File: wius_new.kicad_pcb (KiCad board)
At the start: 6 copper layers, 54 x 28 mm, 134 parts, among them IC1 BQ24040DSQT, J2 52746-1271, J3 1040310811, J4 SS5-10-3.00-L-D-K-TR, J5 USB4745-03-A, J8 2, J9 U.FL, M1 MountingHole_Pad, M2 MountingHole_Pad, M3 MountingHole_Pad, M4 MountingHole_Pad, SW3 Button Switch SPST-No, SW4 Button Switch SPST-No, U1 TPS62840YBGR, U12 SN74LVC1T45DCK, U13 TXB0104RUT, U2 TXB0104RUT, U3 SiWG917Y, U4 FT232HPQ, U5 LSM6DSV, U6 SN74AXC4T774RSVR, U7 SOIC_clipProgSmall, U8 TXB0104RUT, U9 PCAL6408AHK, Y1 SIT1552AI-JE-DCC-32.768E

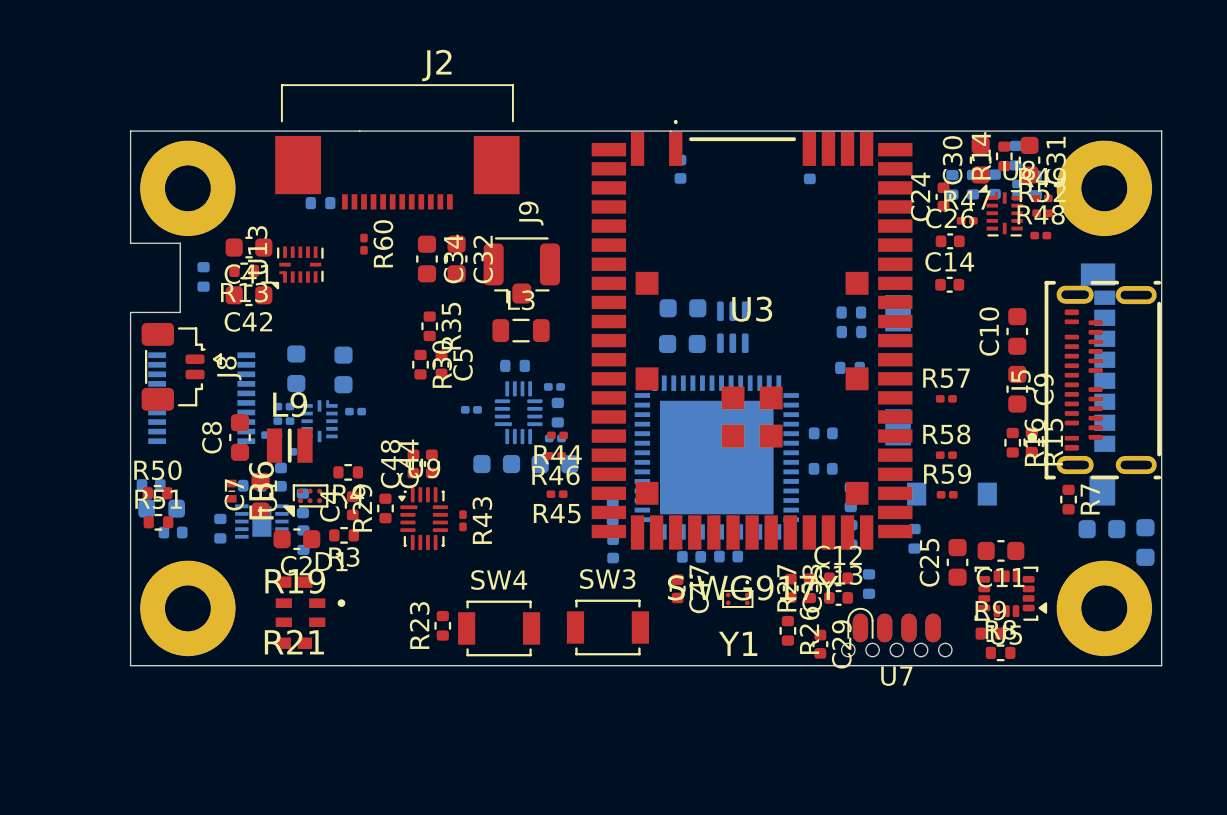
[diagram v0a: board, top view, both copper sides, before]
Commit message: initial routing of SPI, USB and Power
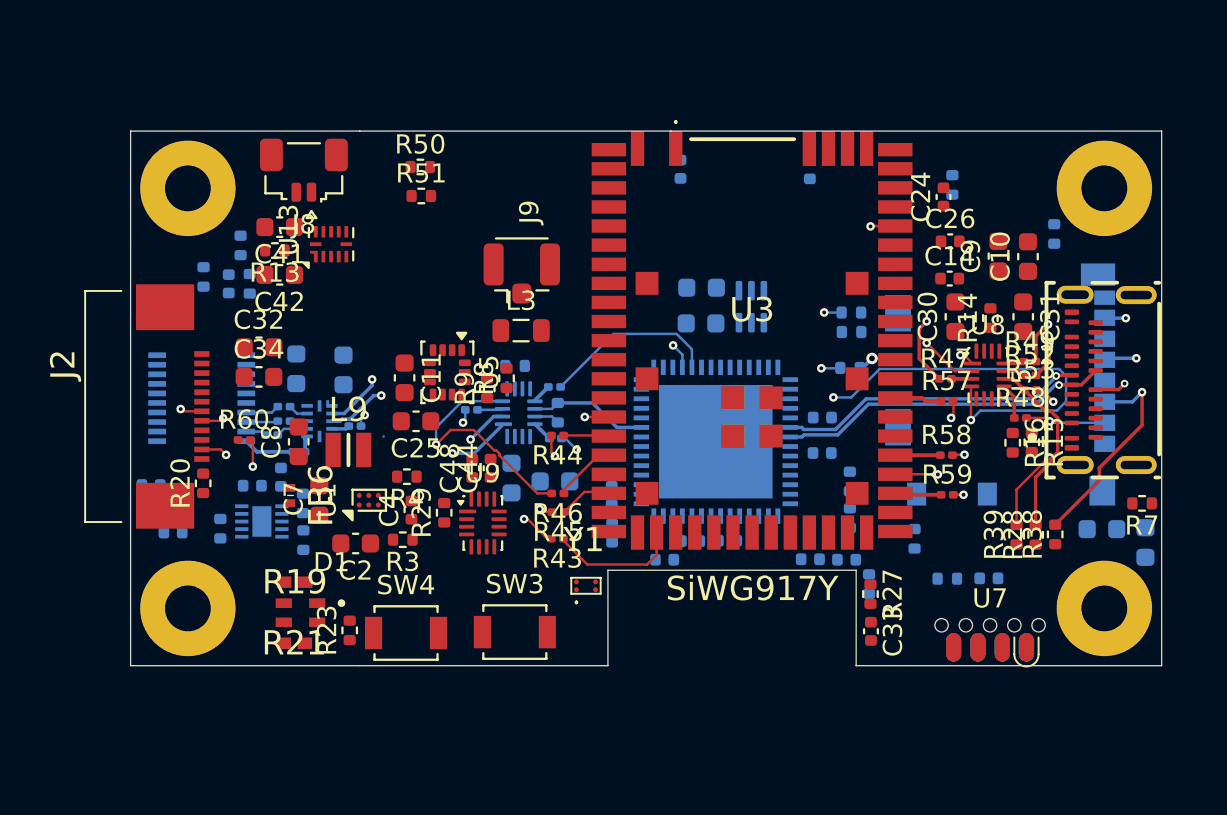
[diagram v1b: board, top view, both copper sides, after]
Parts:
- removed R40: 100k, Resistor_SMD:R_0402_1005Metric
- added R28: 10k, Resistor_SMD:R_0402_1005Metric, F.Cu at (170.4, 107.2)
- C12, C13, C29, C47, C5, R26, R30, R35: moved to B.Cu
- R20, R53: moved to F.Cu
- R38, R39: value 100k -> 10k; moved to F.Cu
- U8: value TXB0104RUT -> SN74AXC4T774RSVR; footprint Package_DFN_QFN:Texas_R-PUQFN-N12 -> Package_DFN_QFN:UQFN-16_1.8x2.6mm_P0.4mm
- moved C11 32.5 mm to (137.3, 98.9), turned to -90 degrees
- moved U5 31.5 mm to (139.6, 98.6), turned to -90 degrees
- moved R8 29.6 mm to (142.7, 98.9), turned to 90 degrees
- moved R9 29.3 mm to (141.7, 99.5), turned to 90 degrees
- moved C25 29.3 mm to (137.9, 101.2), turned to 180 degrees
- moved R50 21.9 mm to (138.2, 87.9)
- moved R51 21.9 mm to (138.2, 89.4)
- moved R38 19.9 mm to (171.4, 107.1), turned to 90 degrees
- moved J2 19.1 mm to (123.7, 100.4), turned to -90 degrees
- moved R39 18.4 mm to (169.4, 107.1), turned to 90 degrees
- moved R20 15.9 mm to (126.8, 104.5), turned to 90 degrees
- moved J8 12.4 mm to (132.1, 88.0), turned to 180 degrees
- moved R60 12.0 mm to (128.9, 102.2), turned to 0 degrees
- moved C5 11.9 mm to (128.1, 94.0)
- moved C32 11.3 mm to (129.7, 97.3), turned to 0 degrees
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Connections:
- R14 pad 1: /IMU_SD/SD_EN -> VIO
- R14 pad 2: GND -> /IMU_SD/SD_EN
- R38 pad 2: /IMU_SD/SPI_SD.MISO -> /IMU_SD/SPI_SD.MOSI
- R39 pad 2: /IMU_SD/SPI_SD.MOSI -> /IMU_SD/SPI_SD.CS0
- U8 pad 1: VIO -> /IMU_SD/SPI_MCU.SCK
- U8 pad 10: Net-(U8-B1) -> /IMU_SD/SPI_SD.MISO
- U8 pad 11: 3V3_VBUS -> Net-(U8-B2)
- U8 pad 12: /IMU_SD/SD_EN -> Net-(U8-B1)
- U8 pad 2: /IMU_SD/SPI_MCU.SCK -> /IMU_SD/SPI_MCU.MOSI
- U8 pad 3: /IMU_SD/SPI_MCU.MOSI -> Net-(U8-A3)
- U8 pad 4: Net-(U8-A3) -> /IMU_SD/SPI_MCU.CS0
- U8 pad 5: /IMU_SD/SPI_MCU.CS0 -> GND
- U8 pad 6: GND -> VIO
- U8 pad 7: Net-(U8-B4) -> /IMU_SD/SD_EN
- U8 pad 8: /IMU_SD/SPI_SD.MISO -> GND
- U8 pad 9: Net-(U8-B2) -> Net-(U8-B4)
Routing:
- net 3V3_VBUS: track 0.00 -> 95.7 mm
- net VIO: track 0.00 -> 86.8 mm
- net /MCU/ULP_SSI.CS0: track 0.00 -> 55.0 mm, vias 0 -> 2
- net 1V8: track 0.00 -> 49.5 mm
- net /MCU/ULP_SSI.SCK: track 0.00 -> 45.4 mm, vias 0 -> 2
- net /MCU/ULP_SSI.MOSI: track 0.00 -> 44.7 mm, vias 0 -> 2
- net /MCU/ULP_SSI.MISO: track 0.00 -> 43.5 mm, vias 0 -> 2
- net /IMU_SD/SPI_MCU.CS0: track 0.00 -> 38.8 mm, vias 0 -> 3
- net /IMU_SD/SPI_MCU.SCK: track 0.00 -> 38.2 mm, vias 0 -> 3
- net /IMU_SD/SPI_MCU.MOSI: track 0.00 -> 34.9 mm, vias 0 -> 3
- net 5V: track 0.00 -> 34.6 mm
- net /IMU_SD/SPI_MCU.MISO: track 0.00 -> 34.3 mm, vias 0 -> 3
- net /MCU/SPI_FPGA.MISO: track 0.00 -> 34.2 mm, vias 0 -> 2
- net /MCU/SPI_FPGA.MOSI: track 0.00 -> 32.6 mm, vias 0 -> 2
- net /MCU/SPI_FPGA.SCK: track 0.00 -> 30.2 mm, vias 0 -> 2
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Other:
- outline, holes or cut-outs redrawn

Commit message: Comments on layout
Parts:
- removed U5: LSM6DSV, Package_LGA:LGA-14_3x2.5mm_P0.5mm_LayoutBorder3x4y
- J2: moved to B.Cu
- moved J2 43.9 mm to (165.5, 87.0), turned to 0 degrees
- moved R60 40.6 mm to (167.4, 89.2)
- moved R23 30.9 mm to (164.8, 118.0)
- moved SW4 28.5 mm to (165.6, 108.1), turned to 180 degrees
- moved U12 18.0 mm to (169.3, 83.6)
- moved C37 18.0 mm to (166.7, 82.6)
- moved C38 18.0 mm to (166.7, 84.5)
- moved R54 17.4 mm to (157.5, 95.8), turned to 180 degrees
- moved C47 13.2 mm to (157.6, 97.0), turned to 0 degrees
- moved U6 12.8 mm to (155.1, 95.6), turned to 180 degrees
- moved R31 12.1 mm to (155.2, 98.0), turned to 180 degrees
- moved R38 11.2 mm to (170.4, 96.0), turned to -90 degrees
- moved R55 11.1 mm to (153.1, 94.2), turned to 180 degrees
- moved R16 10.8 mm to (174.4, 92.9), turned to 90 degrees
- moved R15 9.93 mm to (173.4, 92.9), turned to 90 degrees
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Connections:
- R32 pad 1: /MCU/SPI_FPGA.MOSI -> /IMU_SD/SPI_MCU.MOSI
- R33 pad 1: /MCU/SPI_FPGA.SCK -> /IMU_SD/SPI_MCU.SCK
- R34 pad 1: /MCU/SPI_FPGA.CS0 -> /IMU_SD/SPI_MCU.CS0
- R43 pad 2: /IMU_SD/SPI_MCU.SCK -> /MCU/SPI_FPGA.SCK
- R44 pad 2: /IMU_SD/SPI_MCU.CS0 -> /MCU/SPI_FPGA.CS0
- R45 pad 2: /IMU_SD/SPI_MCU.MOSI -> /MCU/SPI_FPGA.MOSI
- R46 pad 1: Net-(U3C-GPIO_54) -> Net-(U3C-GPIO_29)
- U3 pad 17: /IMU_SD/SPI_MCU.MISO -> /MCU/SPI_FPGA.MISO
- U3 pad 19: Net-(U3C-GPIO_54) -> unconnected-(U3C-GPIO_54-Pad19)
- U3 pad 47: unconnected-(U3C-GPIO_29-Pad47) -> Net-(U3C-GPIO_29)
- U3 pad 53: /MCU/SPI_FPGA.MISO -> /IMU_SD/SPI_MCU.MISO
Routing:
- net /MCU/ULP_SSI.CS0: track 55.0 -> 1.69 mm, vias 2 -> 1
- net /MCU/ULP_SSI.SCK: track 45.4 -> 2.15 mm, vias 2 -> 1
- net /MCU/ULP_SSI.MOSI: track 44.7 -> 2.03 mm, vias 2 -> 1
- net /MCU/ULP_SSI.MISO: track 43.5 -> 3.69 mm, vias 2 -> 1
- net /IMU_SD/SPI_MCU.SCK: track 38.2 -> 0.83 mm, vias 3 -> 1
- net /IMU_SD/SPI_MCU.MOSI: track 34.9 -> 1.99 mm, vias 3 -> 1
- net /IMU_SD/SPI_MCU.MISO: track 34.3 -> 3.86 mm, vias 3 -> 1
- net /MCU/SPI_FPGA.MISO: track 34.2 -> 13.2 mm
- net /IMU_SD/SPI_MCU.CS0: track 38.8 -> 20.5 mm, vias 3 -> 1
- net /MCU/SPI_FPGA.MOSI: track 32.6 -> 15.9 mm
- net /MCU/SPI_FPGA.SCK: track 30.2 -> 16.9 mm
- net /USB_FT232HPQ/USB_D_P: track 17.6 -> 4.89 mm
- net /USB_FT232HPQ/USB_D_N: track 21.5 -> 8.79 mm
- net /MCU/SPI_FPGA.CS0: track 0.01 -> 12.4 mm, vias 0 -> 2
- net 3V3_VBUS: track 95.7 -> 86.8 mm
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- added copper zone on In3.Cu, net GND
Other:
- board size 54 x 28 mm -> 55.4 x 33.8 mm

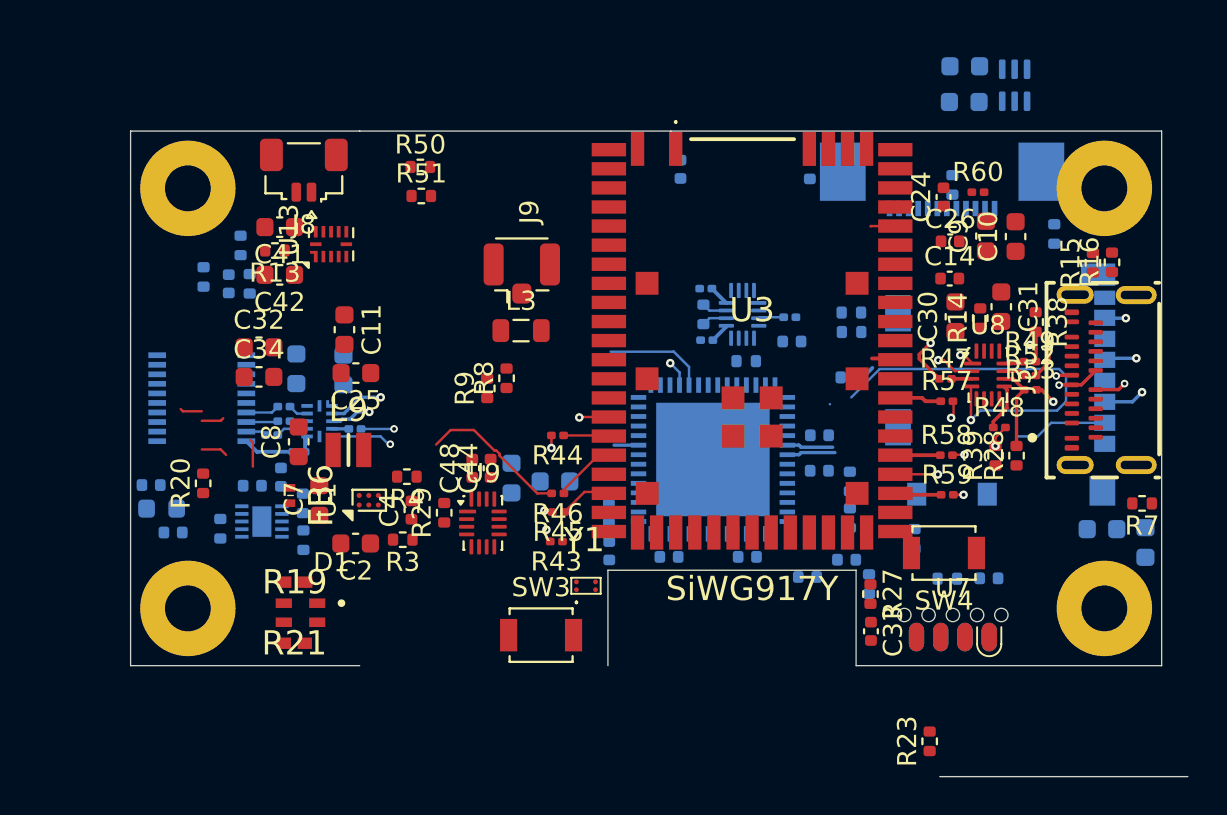
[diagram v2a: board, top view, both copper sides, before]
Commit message: updated routing SPI, change 0402 to 0201
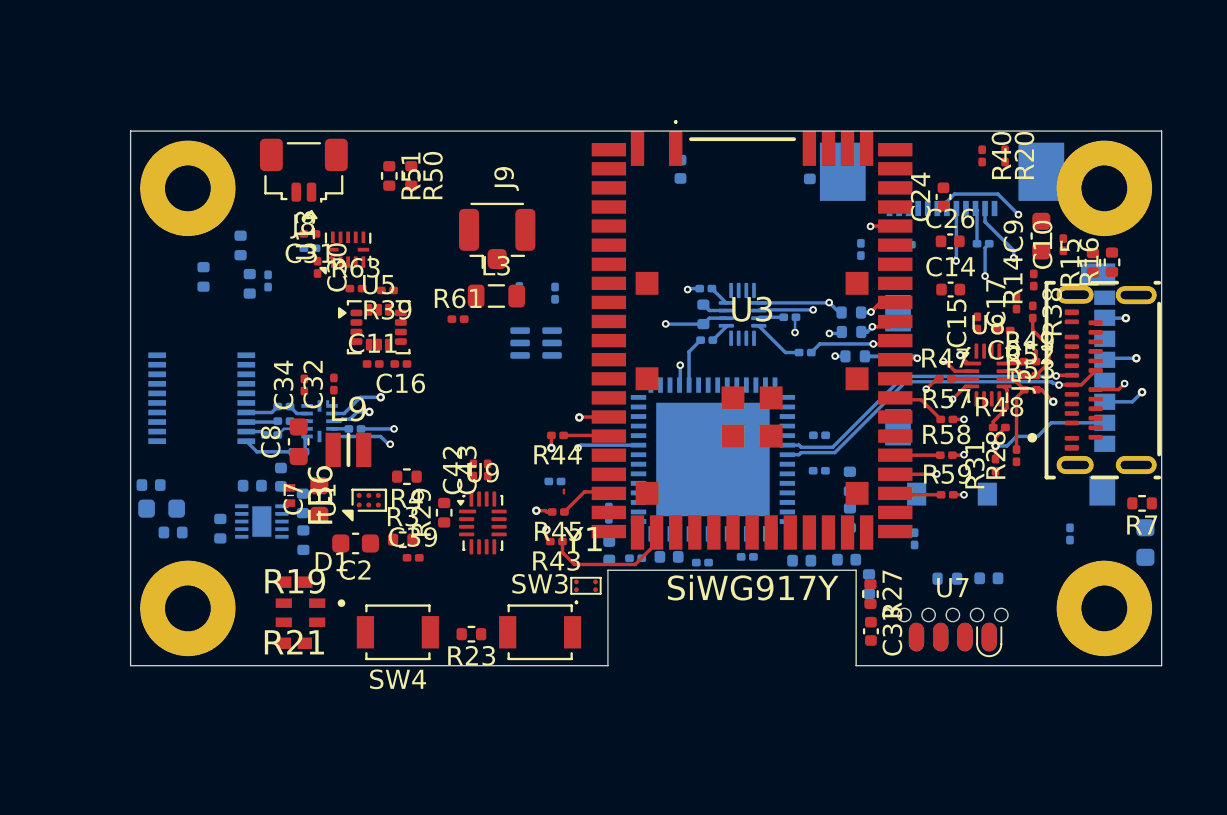
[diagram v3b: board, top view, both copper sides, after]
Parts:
- removed C4, C44, C47, C48, C5: 100nF, Capacitor_SMD:C_0402_1005Metric
- removed R10, R11, R8, R9: 10k, Resistor_SMD:R_0402_1005Metric
- added C15: 100nF, Capacitor_SMD:C_0201_0603Metric, F.Cu at (167.3, 96.0)
- added C16: 100nF, Capacitor_SMD:C_0201_0603Metric, F.Cu at (137.2, 98.2)
- added C17: 100nF, Capacitor_SMD:C_0201_0603Metric, F.Cu at (169.4, 95.0)
- added C43: 100nF, Capacitor_SMD:C_0201_0603Metric, F.Cu at (141.7, 103.8)
- added C6: 100nF, Capacitor_SMD:C_0201_0603Metric, F.Cu at (168.8, 96.5)
- added R40: 100k, Resistor_SMD:R_0201_0603Metric, F.Cu at (167.6, 87.3)
- added R61: 100k, Resistor_SMD:R_0201_0603Metric, F.Cu at (140.2, 95.8)
- added R62: 100k, Resistor_SMD:R_0201_0603Metric, B.Cu at (132.4, 92.1)
- added R63: 10k, Resistor_SMD:R_0201_0603Metric, F.Cu at (134.8, 94.2)
- added U5: LSM6DSV, Package_LGA:LGA-14_3x2.5mm_P0.5mm_LayoutBorder3x4y, F.Cu at (136.0, 96.3)
- C10, C11, C28, C30, C31, C32, C34, C35, C36, C37, C38, C40, C42: footprint Capacitor_SMD:C_0603_1608Metric -> Capacitor_SMD:C_0201_0603Metric
- C18, C20, C21, C22: footprint Capacitor_SMD:C_0402_1005Metric -> Capacitor_SMD:C_0201_0603Metric
- C25, C41: footprint Capacitor_SMD:C_0603_1608Metric -> Capacitor_SMD:C_0201_0603Metric; moved to B.Cu
- C39: footprint Capacitor_SMD:C_0603_1608Metric -> Capacitor_SMD:C_0201_0603Metric; moved to F.Cu
- R13: value 100k -> 10k; footprint Resistor_SMD:R_0402_1005Metric -> Resistor_SMD:R_0201_0603Metric; moved to B.Cu
- R14: value 100k -> 10k; footprint Resistor_SMD:R_0402_1005Metric -> Resistor_SMD:R_0201_0603Metric
- R17, R20, R28, R38, R39: footprint Resistor_SMD:R_0402_1005Metric -> Resistor_SMD:R_0201_0603Metric
- R31: value 100k -> 10k; footprint Resistor_SMD:R_0402_1005Metric -> Resistor_SMD:R_0201_0603Metric; moved to F.Cu
- R46, R60: moved to B.Cu
- moved R20 45.4 mm to (168.8, 87.3), turned to -90 degrees
- moved R13 44.2 mm to (172.2, 107.1), turned to 90 degrees
- moved C31 36.4 mm to (132.4, 91.4), turned to 180 degrees
- moved C30 33.5 mm to (132.8, 93.1), turned to -90 degrees
- moved R39 33.0 mm to (136.5, 94.3), turned to 180 degrees
- moved SW4 28.9 mm to (137.0, 112.2)
- moved U12 28.5 mm to (144.2, 97.1), turned to 180 degrees
- moved C41 28.3 mm to (152.9, 108.6), turned to 0 degrees
- moved C25 27.2 mm to (161.2, 92.2), turned to -90 degrees
- moved C38 25.3 mm to (143.4, 94.5), turned to 90 degrees
- moved R23 24.6 mm to (140.8, 112.3), turned to 180 degrees
- moved C37 24.5 mm to (145.2, 94.5), turned to 90 degrees
- moved C28 18.1 mm to (163.6, 92.0)
- moved R46 14.9 mm to (158.3, 97.6)
- moved C42 14.4 mm to (140.9, 103.8), turned to 90 degrees
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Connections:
- C25 pad 1: VIO -> VBATTERY
- C28 pad 1: 3V3_VBUS -> VIO
- C32 pad 1: VBATTERY -> VIO
- C34 pad 1: VIO -> 3V3_VBUS
- C39 pad 1: VIO -> Net-(U1-EN)
- C40 pad 1: 3V3_VBUS -> /MCU/BATT_SENSE
- C41 pad 1: 3V3_VBUS -> VIO
- R13 pad 1: /MCU/FPGA_EN -> 3V3_VBUS
- R13 pad 2: GND -> Net-(J3-DAT2)
- R14 pad 1: VIO -> 3V3_VBUS
- R14 pad 2: /IMU_SD/SD_EN -> Net-(J3-DAT1)
- R31 pad 1: VIO -> 3V3_VBUS
- R31 pad 2: /MCU/FT_EN -> /IMU_SD/SPI_SD.CS0
- R39 pad 1: 3V3_VBUS -> VIO
- R39 pad 2: /IMU_SD/SPI_SD.CS0 -> /IMU_SD/I2C_IMU.SCL
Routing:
- net 3V3_VBUS: track 86.8 -> 175.3 mm
- net VBATTERY: track 29.1 -> 75.3 mm
- net VIO: track 86.8 -> 109.6 mm
- net /USB_FT232HPQ/1V2: track 21.5 -> 0.00 mm
- net /MCU/ULP_SSI.CS0: track 1.69 -> 21.2 mm, vias 1 -> 2
- net /MCU/ULP_SSI.MOSI: track 2.03 -> 17.1 mm, vias 1 -> 2
- net /IMU_SD/SPI_MCU.MISO: track 3.86 -> 18.4 mm, vias 1 -> 3
- net 5V: track 34.6 -> 47.9 mm
- net /USB_FT232HPQ/USB_D_N: track 8.79 -> 22.0 mm
- net /USB_FT232HPQ/USB_D_P: track 4.89 -> 18.1 mm
- net /MCU/ULP_SSI.MISO: track 3.69 -> 16.8 mm, vias 1 -> 2
- net /IMU_SD/SPI_MCU.SCK: track 0.83 -> 13.9 mm, vias 1 -> 2
- net /USB_FT232HPQ/SPI_FT232.MIOSI0: track 2.61 -> 14.9 mm, vias 0 -> 2
- net /IMU_SD/SPI_MCU.MOSI: track 1.99 -> 14.2 mm, vias 1 -> 3
- net /MCU/ULP_SSI.SCK: track 2.15 -> 12.3 mm, vias 1 -> 2
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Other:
- board size 55.4 x 33.8 mm -> 54 x 28 mm

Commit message: Add comments from layout meeting 20.07.2026
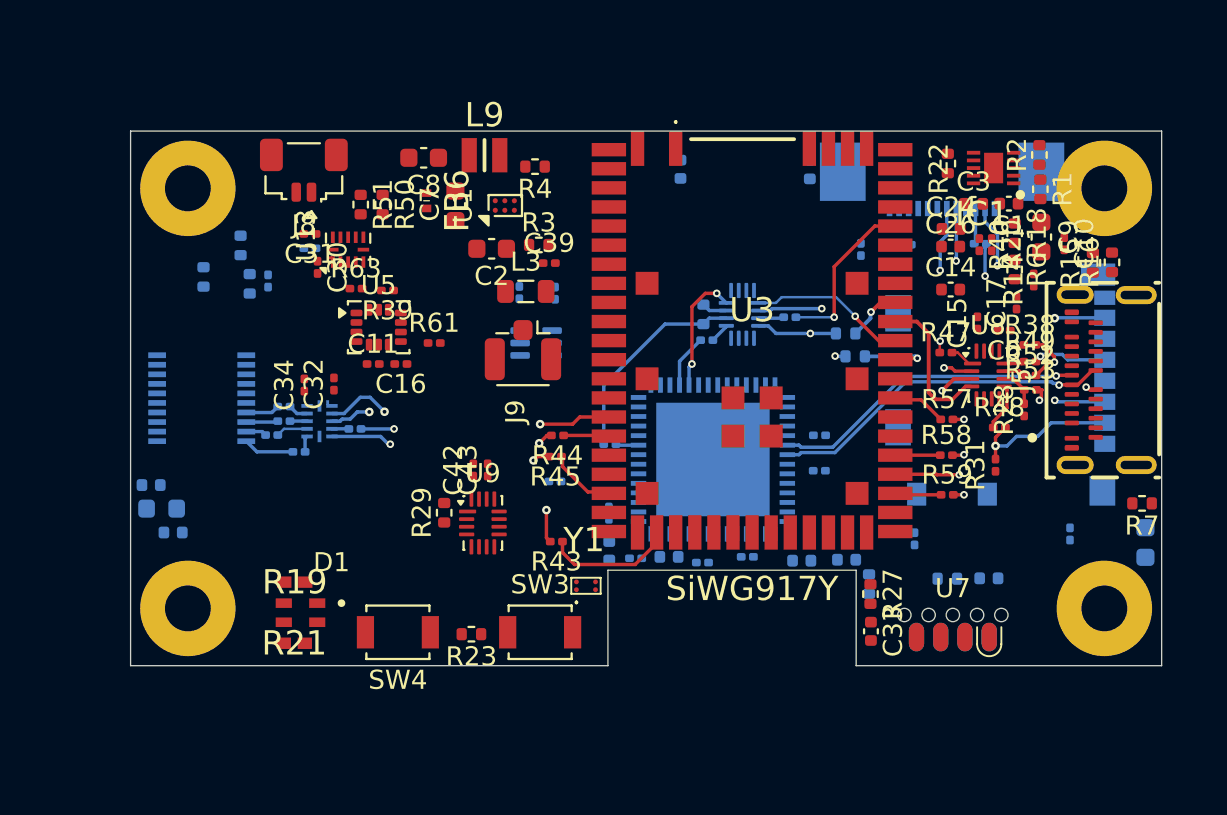
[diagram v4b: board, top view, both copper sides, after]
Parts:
- removed R34: 22, Resistor_SMD:R_0402_1005Metric
- removed R46: 22, Resistor_SMD:R_0201_0603Metric
- C1, C3, IC1, R1, R18, R2, R22, R6: moved to F.Cu
- moved R2 43.5 mm to (170.6, 87.2), turned to 90 degrees
- moved R22 42.6 mm to (165.8, 87.7), turned to 90 degrees
- moved IC1 42.6 mm to (168.2, 87.9)
- moved R1 42.0 mm to (170.7, 89.0), turned to -90 degrees
- moved C1 40.7 mm to (169.0, 89.8), turned to 180 degrees
- moved C3 40.6 mm to (167.2, 89.8)
- moved R4 17.6 mm to (144.2, 87.9)
- moved L9 17.0 mm to (141.5, 87.3)
- moved R3 17.0 mm to (144.4, 92.0)
- moved C2 17.0 mm to (141.9, 92.2)
- moved C39 17.0 mm to (144.9, 92.9)
- moved C7 17.0 mm to (140.0, 89.9)
- moved FB6 17.0 mm to (138.5, 89.7)
- moved U1 17.0 mm to (142.6, 89.9)
- moved C8 16.3 mm to (138.3, 87.4), turned to 180 degrees
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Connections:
- C24 pad 1: 1V8 -> /MCU/MCU_POWER_RF/Flash_IO_VDD
- R47 pad 2: Net-(U8-A3) -> Net-(U8-A1)
- R49 pad 1: Net-(U8-B1) -> Net-(U8-B3)
- R55 pad 1: Net-(U6-B1) -> Net-(U4A-ADBUS0)
- R55 pad 2: /USB_FT232HPQ/SPI_FT232.SCK -> /USB_FT232HPQ/SPI_FT232.MIOSI0
- R56 pad 2: /USB_FT232HPQ/SPI_FT232.CS -> /USB_FT232HPQ/SPI_FT232.SCK
- U3 pad 36: unconnected-(U3A-1V8_LDO-Pad36) -> /MCU/MCU_POWER_RF/Flash_IO_VDD
- U3 pad 47: Net-(U3C-GPIO_29) -> /IMU_SD/SPI_MCU.CS1
- U3 pad 48: Net-(U3C-GPIO_28) -> /IMU_SD/SPI_MCU.CS0
- U3 pad 54: 1V8 -> /MCU/MCU_POWER_RF/Flash_IO_VDD
- U4 pad 23: /USB_FT232HPQ/SPI_FT232.MIOSI0 -> Net-(U4A-ADBUS0)
- U6 pad 1: /IMU_SD/SPI_MCU.SCK -> /IMU_SD/SPI_MCU.CS1
- U6 pad 12: Net-(U6-B1) -> /USB_FT232HPQ/SPI_FT232.CS
- U6 pad 4: /IMU_SD/SPI_MCU.CS1 -> /IMU_SD/SPI_MCU.SCK
- U8 pad 1: /IMU_SD/SPI_MCU.SCK -> Net-(U8-A1)
- U8 pad 10: /IMU_SD/SPI_SD.MISO -> Net-(U8-B3)
- U8 pad 12: Net-(U8-B1) -> /IMU_SD/SPI_SD.MISO
- U8 pad 15: VIO -> GND
- U8 pad 3: Net-(U8-A3) -> /IMU_SD/SPI_MCU.SCK
- U8 pad 5: GND -> VIO
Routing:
- net /IMU_SD/SPI_MCU.CS1: track 2.69 -> 183.7 mm, vias 0 -> 1
- net 3V3_VBUS: track 175.3 -> 0.00 mm
- net VIO: track 109.6 -> 0.59 mm
- net 1V8: track 55.4 -> 0.00 mm
- net 5V: track 47.9 -> 7.18 mm
- net /MCU/SPI_FPGA.MOSI: track 15.9 -> 43.8 mm
- net VBATTERY: track 75.3 -> 54.4 mm
- net /IMU_SD/SPI_SD.SCK: track 9.54 -> 3.90 mm, vias 2 -> 1
- net Net-(U3C-GPIO_29): track 4.85 -> 0.00 mm, vias 1 -> 0
- net /MCU/ULP_SSI.CS0: track 21.2 -> 16.6 mm
- net /IMU_SD/SPI_SD.MOSI: track 11.8 -> 7.73 mm
- net /USB_FT232HPQ/SPI_FT232.MIOSI0: track 14.9 -> 11.0 mm, vias 2 -> 0
- net /USB_FT232HPQ/SPI_FT232.CS: track 2.60 -> 6.47 mm, vias 0 -> 2
- net Net-(J3-DAT0): track 12.5 -> 8.64 mm
- net /IMU_SD/SPI_MCU.CS0: track 11.1 -> 7.78 mm, vias 2 -> 0
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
